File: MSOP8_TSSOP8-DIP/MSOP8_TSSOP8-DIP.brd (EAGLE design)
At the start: 10.8 x 13.3 mm, 2 parts, among them U1 DUMMY8

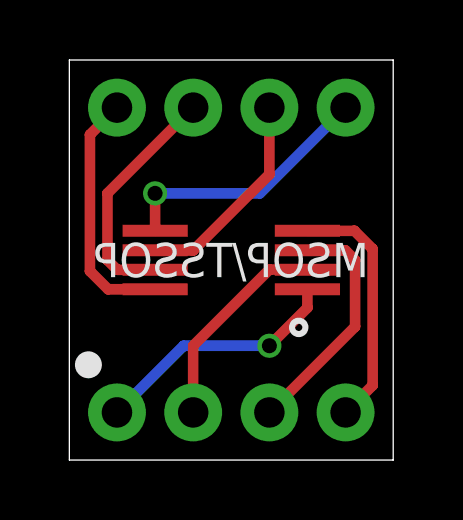
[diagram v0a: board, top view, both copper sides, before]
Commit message: msop/tssop update
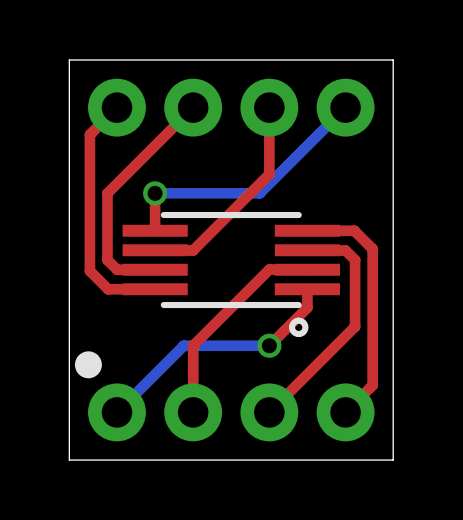
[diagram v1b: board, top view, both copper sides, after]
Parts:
- renumbered MSOP/TSSOP to MSOP/TSSOP8
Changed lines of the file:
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@@
 <?xml version="1.0" encoding="utf-8"?>
 <!DOCTYPE eagle SYSTEM "eagle.dtd">
-<eagle version="8.4.3">
+<eagle version="8.5.2">
 <drawing>
 <settings>
@@
 <param name="checkRestrict" value="0"/>
 <param name="checkStop" value="0"/>
+<param name="checkValues" value="0"/>
 <param name="useDiameter" value="13"/>
 <param name="maxErrors" value="50"/>
@@
 <elements>
 <element name="U1" library="my-ic" package="MSOP8-TSSOP8" value="DUMMY8" x="5.3975" y="6.6675" smashed="yes" rot="R90"/>
-<element name="MSOP/TSSOP" library="my-pinhead" package="ADAPTER-8" value="ADAPTER-8" x="0" y="0" smashed="yes">
-<attribute name="NAME" x="5.3975" y="6.6675" size="1.143" layer="25" ratio="16" rot="MR0" align="center"/>
+<element name="MSOP/TSSOP8" library="my-pinhead" package="ADAPTER-8" value="ADAPTER-8" x="0" y="0" smashed="yes">
+<attribute name="NAME" x="5.3975" y="6.6675" size="1.016" layer="22" ratio="16" rot="MR0" align="center"/>
 </element>
 </elements>
 <signals>
 <signal name="N$1">
-<contactref element="MSOP/TSSOP" pad="1"/>
+<contactref element="MSOP/TSSOP8" pad="1"/>
 <contactref element="U1" pad="1"/>
 <via x="6.6675" y="3.81" extent="1-16" drill="0.5"/>
@@
 </signal>
 <signal name="N$2">
-<contactref element="MSOP/TSSOP" pad="2"/>
+<contactref element="MSOP/TSSOP8" pad="2"/>
 <contactref element="U1" pad="2"/>
 <wire x1="4.1275" y1="1.5875" x2="4.1275" y2="3.81" width="0.3556" layer="1"/>
@@
 </signal>
 <signal name="N$3">
-<contactref element="MSOP/TSSOP" pad="3"/>
+<contactref element="MSOP/TSSOP8" pad="3"/>
 <contactref element="U1" pad="3"/>
 <wire x1="6.6675" y1="1.5875" x2="9.525" y2="4.445" width="0.3556" layer="1"/>
@@
 </signal>
 <signal name="N$4">
-<contactref element="MSOP/TSSOP" pad="4"/>
+<contactref element="MSOP/TSSOP8" pad="4"/>
 <contactref element="U1" pad="4"/>
 <wire x1="7.935" y1="7.6425" x2="9.5025" y2="7.6425" width="0.3556" layer="1"/>
@@
 <signal name="N$5">
 <contactref element="U1" pad="5"/>
-<contactref element="MSOP/TSSOP" pad="5"/>
+<contactref element="MSOP/TSSOP8" pad="5"/>
 <wire x1="2.86" y1="7.6425" x2="2.86" y2="8.8875" width="0.3556" layer="1"/>
 <wire x1="2.86" y1="8.8875" x2="2.8575" y2="8.89" width="0.3556" layer="1"/>
@@
 <signal name="N$6">
 <contactref element="U1" pad="6"/>
-<contactref element="MSOP/TSSOP" pad="6"/>
+<contactref element="MSOP/TSSOP8" pad="6"/>
 <wire x1="6.6675" y1="11.7475" x2="6.6675" y2="9.525" width="0.3556" layer="1"/>
 <wire x1="6.6675" y1="9.525" x2="4.1275" y2="6.985" width="0.3556" layer="1"/>
@@
 <signal name="N$7">
 <contactref element="U1" pad="7"/>
-<contactref element="MSOP/TSSOP" pad="7"/>
+<contactref element="MSOP/TSSOP8" pad="7"/>
 <wire x1="2.86" y1="6.3425" x2="1.595" y2="6.3425" width="0.3556" layer="1"/>
 <wire x1="1.595" y1="6.3425" x2="1.27" y2="6.6675" width="0.3556" layer="1"/>
@@
 <signal name="N$8">
 <contactref element="U1" pad="8"/>
-<contactref element="MSOP/TSSOP" pad="8"/>
+<contactref element="MSOP/TSSOP8" pad="8"/>
 <wire x1="2.86" y1="5.6925" x2="1.2925" y2="5.6925" width="0.3556" layer="1"/>
 <wire x1="1.2925" y1="5.6925" x2="0.6858" y2="6.2992" width="0.3556" layer="1"/>
